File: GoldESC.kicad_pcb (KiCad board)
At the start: 2 copper layers, 2 parts, among them U10 LM5111-1M/NOPB, U20 PSMN1R0-30YLDX

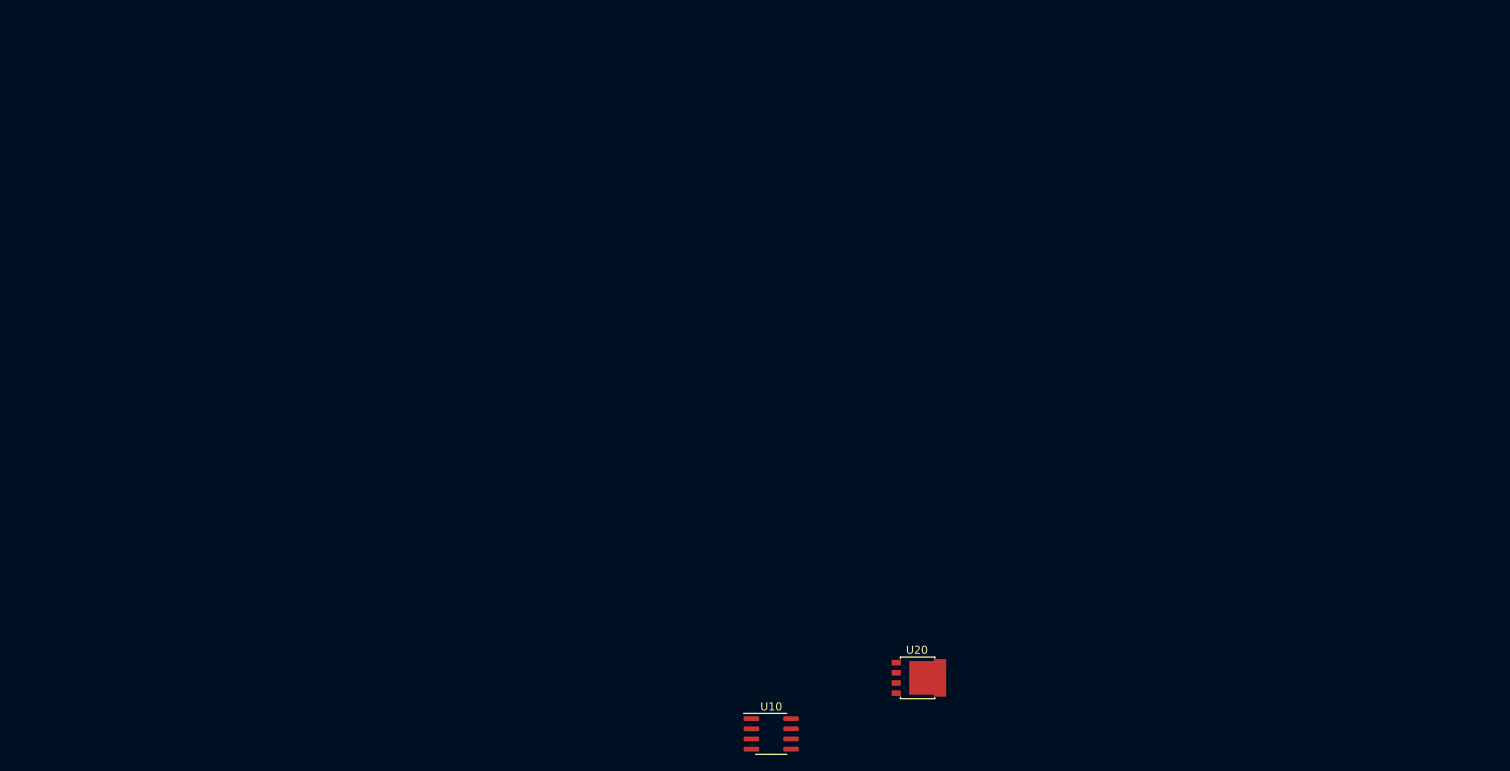
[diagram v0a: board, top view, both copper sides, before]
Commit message: Added fets and drivers, initial critical components selected
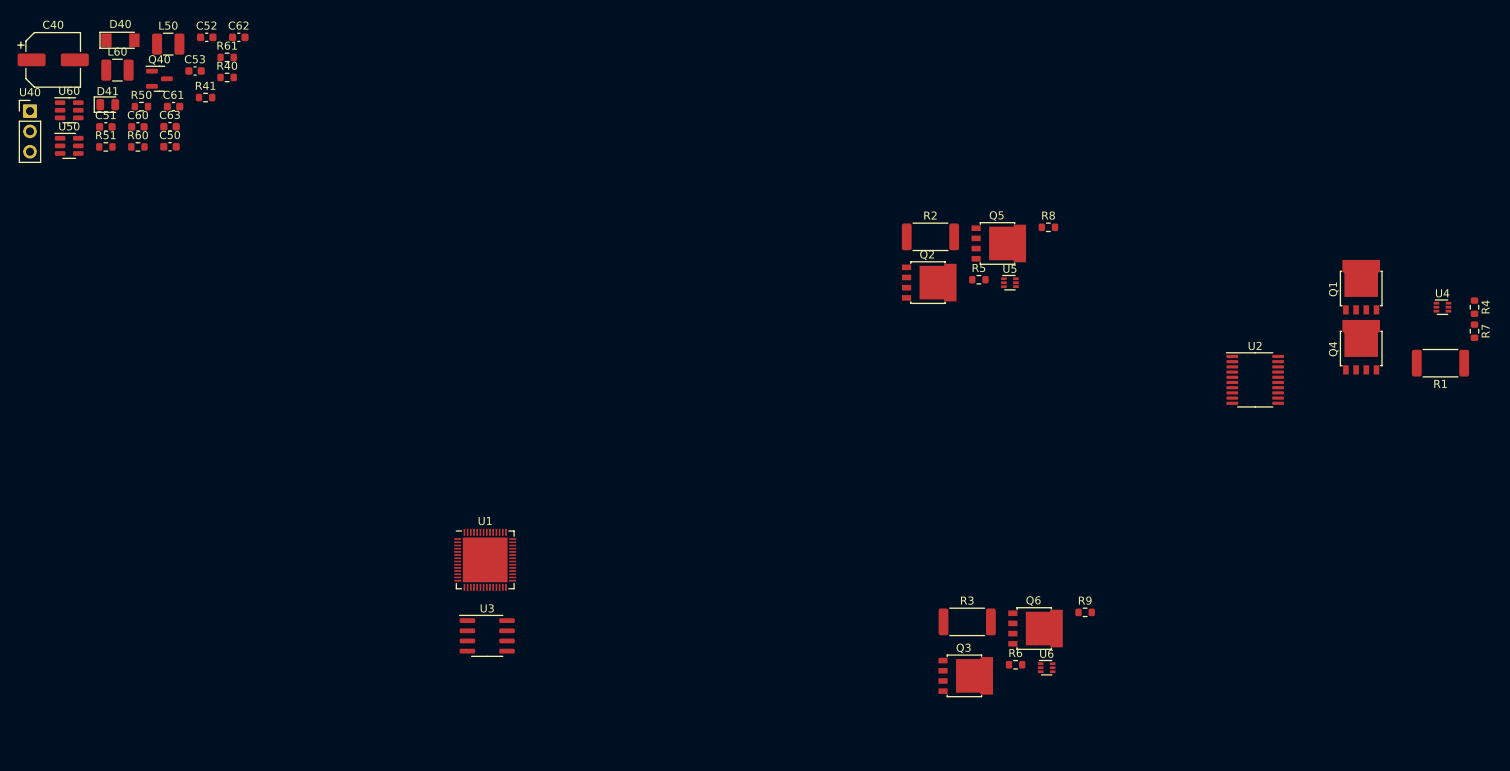
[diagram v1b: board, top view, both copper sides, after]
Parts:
- removed U10: LM5111-1M/NOPB, Package_SO:SOIC-8_3.9x4.9mm_P1.27mm
- removed U20: PSMN1R0-30YLDX, Package_TO_SOT_SMD:LFPAK56
- added C40: 100uF, Capacitor_SMD:CP_Elec_6.3x7.7, F.Cu at (55.2, 11.2)
- added C50: 10uF, Capacitor_SMD:C_0603_1608Metric, F.Cu at (69.8, 22.1)
- added C51: 100nF, Capacitor_SMD:C_0603_1608Metric, F.Cu at (61.8, 19.6)
- added C52: 22pF, Capacitor_SMD:C_0603_1608Metric, F.Cu at (74.4, 8.43)
- added C53: 22uF, Capacitor_SMD:C_0603_1608Metric, F.Cu at (73.0, 12.6)
- added C60: 10uF, Capacitor_SMD:C_0603_1608Metric, F.Cu at (65.8, 19.6)
- added C61: 100nF, Capacitor_SMD:C_0603_1608Metric, F.Cu at (70.3, 17.1)
- added C62: 22pF, Capacitor_SMD:C_0603_1608Metric, F.Cu at (78.5, 8.43)
- added C63: 22uF, Capacitor_SMD:C_0603_1608Metric, F.Cu at (69.8, 19.6)
- added D40: ZMM5V6, Diode_SMD:D_MiniMELF, F.Cu at (63.6, 8.80)
- added D41: POWER_LED, LED_SMD:LED_0805_2012Metric, F.Cu at (62.1, 16.8)
- added L50: 4.7uH, Inductor_SMD:L_1210_3225Metric, F.Cu at (69.6, 9.28)
- added L60: 4.7uH, Inductor_SMD:L_1210_3225Metric, F.Cu at (63.3, 12.5)
- added Q1: YJG150N03A, Package_TO_SOT_SMD:LFPAK56, F.Cu at (218.8, 39.7)
- added Q2: YJG150N03A, Package_TO_SOT_SMD:LFPAK56, F.Cu at (164.8, 39.1)
- added Q3: YJG150N03A, Package_TO_SOT_SMD:LFPAK56, F.Cu at (169.3, 88.2)
- added Q4: YJG150N03A, Package_TO_SOT_SMD:LFPAK56, F.Cu at (218.8, 47.2)
- added Q40: AO3401A, Package_TO_SOT_SMD:SOT-23, F.Cu at (68.5, 13.6)
- added Q5: YJG150N03A, Package_TO_SOT_SMD:LFPAK56, F.Cu at (173.4, 34.2)
- added Q6: YJG150N03A, Package_TO_SOT_SMD:LFPAK56, F.Cu at (178.0, 82.3)
- added R1: 0.5mR, Resistor_SMD:R_2512_6332Metric, F.Cu at (228.7, 49.2)
- added R2: 0.5mR, Resistor_SMD:R_2512_6332Metric, F.Cu at (164.9, 33.4)
- added R3: 0.5mR, Resistor_SMD:R_2512_6332Metric, F.Cu at (169.5, 81.5)
- added R4: R?, Resistor_SMD:R_0603_1608Metric, F.Cu at (232.9, 42.2)
- added R40: 10K, Resistor_SMD:R_0603_1608Metric, F.Cu at (77.0, 13.4)
- added R41: 1K, Resistor_SMD:R_0603_1608Metric, F.Cu at (74.3, 16.0)
- added R5: R?, Resistor_SMD:R_0603_1608Metric, F.Cu at (171.0, 38.7)
- added R50: 100K, Resistor_SMD:R_0603_1608Metric, F.Cu at (66.3, 17.1)
- added R51: 22K, Resistor_SMD:R_0603_1608Metric, F.Cu at (61.8, 22.1)
- added R6: R?, Resistor_SMD:R_0603_1608Metric, F.Cu at (175.6, 86.9)
- added R60: 100K, Resistor_SMD:R_0603_1608Metric, F.Cu at (65.8, 22.1)
- added R61: 13K, Resistor_SMD:R_0603_1608Metric, F.Cu at (77.0, 10.9)
- added R7: R?, Resistor_SMD:R_0603_1608Metric, F.Cu at (232.9, 45.2)
- added R8: R?, Resistor_SMD:R_0603_1608Metric, F.Cu at (179.7, 32.2)
- added R9: R?, Resistor_SMD:R_0603_1608Metric, F.Cu at (184.2, 80.3)
- added U1: ESP32-S2, Package_DFN_QFN:QFN-56-1EP_7x7mm_P0.4mm_EP5.6x5.6mm, F.Cu at (109.2, 73.8)
- added U2: DRV8300NIPWR, Package_SO:TSSOP-20_4.4x6.5mm_P0.65mm, F.Cu at (205.5, 51.2)
- added U3: MCP2551-I-SN, Package_SO:SOIC-8_3.9x4.9mm_P1.27mm, F.Cu at (109.5, 83.2)
- added U4: INA185A, Package_TO_SOT_SMD:SOT-563, F.Cu at (228.9, 42.2)
- added U40: Switch1SPDT, Connector_PinHeader_2.54mm:PinHeader_1x03_P2.54mm_Vertical, F.Cu at (52.4, 17.6)
- added U5: INA185A, Package_TO_SOT_SMD:SOT-563, F.Cu at (174.8, 39.1)
- added U50: SY8113BADC, Package_TO_SOT_SMD:TSOT-23-6, F.Cu at (57.2, 22.0)
- added U6: INA185A, Package_TO_SOT_SMD:SOT-563, F.Cu at (179.4, 87.2)
- added U60: SY8113BADC, Package_TO_SOT_SMD:TSOT-23-6, F.Cu at (57.2, 17.6)

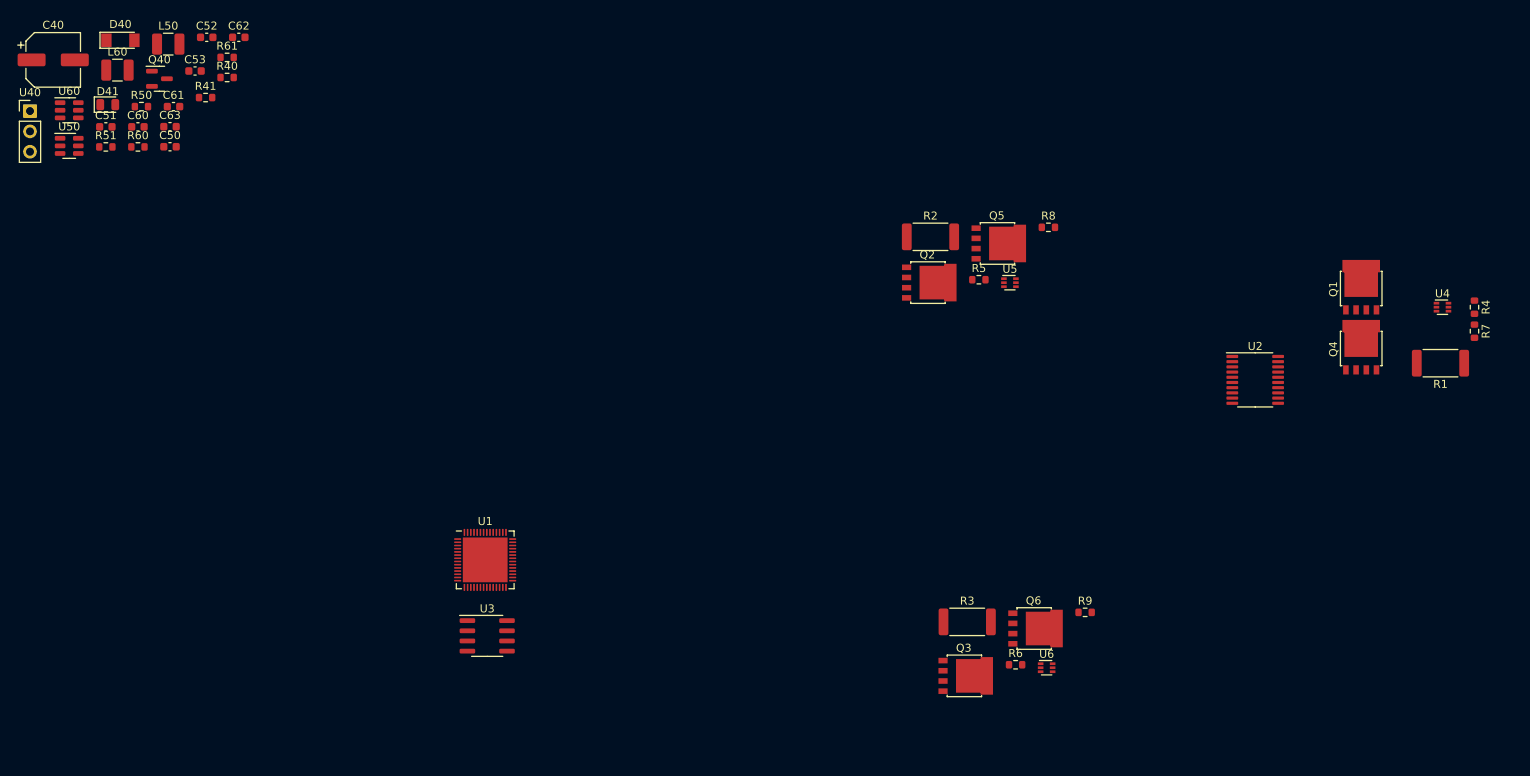
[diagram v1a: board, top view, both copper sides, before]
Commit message: moved the Dsub off-board, most of initial layout routed
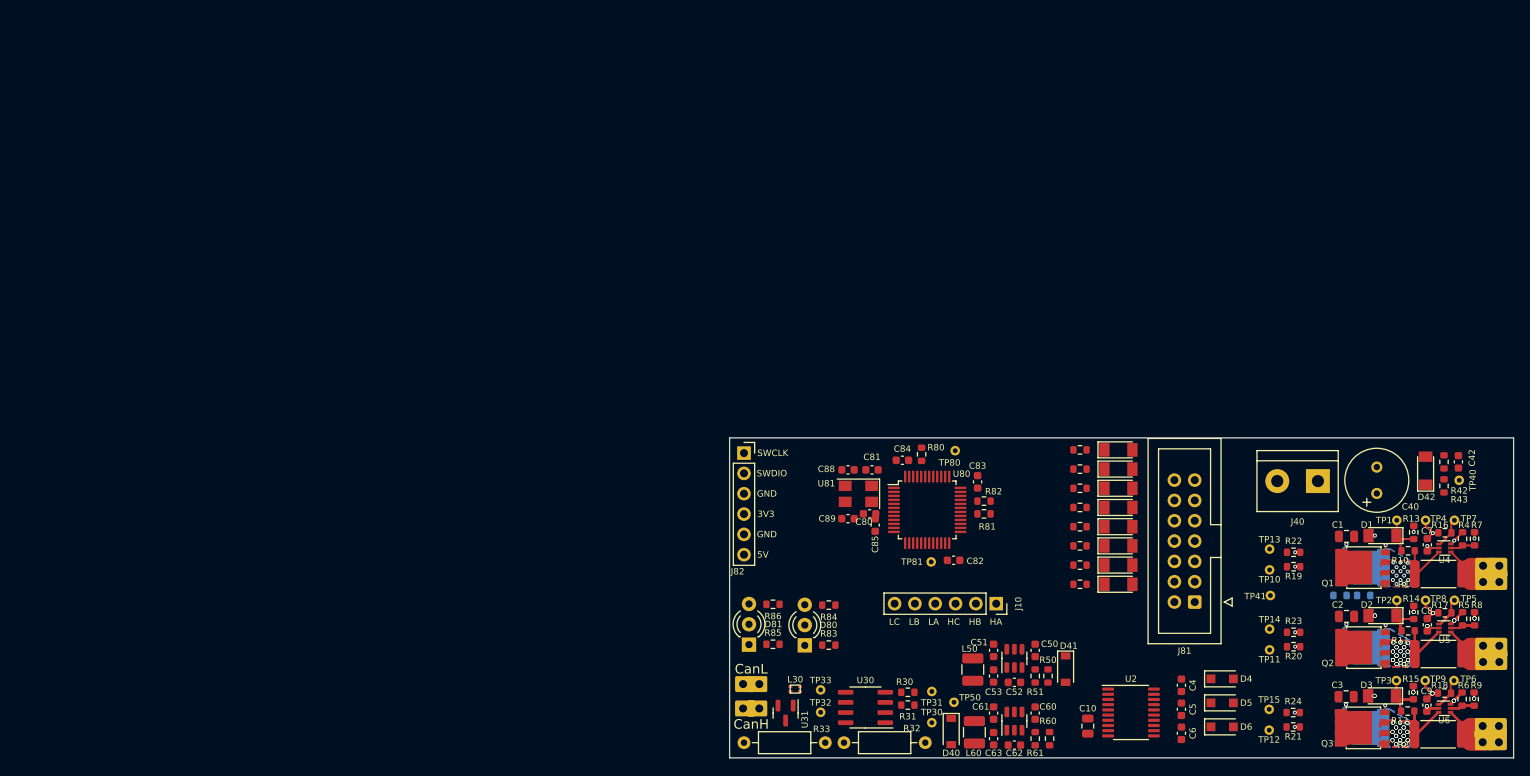
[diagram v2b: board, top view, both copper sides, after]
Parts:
- removed Q40: AO3401A, Package_TO_SOT_SMD:SOT-23
- removed U1: ESP32-S2, Package_DFN_QFN:QFN-56-1EP_7x7mm_P0.4mm_EP5.6x5.6mm
- removed U3: MCP2551-I-SN, Package_SO:SOIC-8_3.9x4.9mm_P1.27mm
- removed U40: Switch1SPDT, Connector_PinHeader_2.54mm:PinHeader_1x03_P2.54mm_Vertical
- added C1: 10uF,25V, Capacitor_SMD:C_0805_2012Metric, F.Cu at (216.9, 70.8)
- added C10: 1uF?/24V?, Capacitor_SMD:C_0805_2012Metric, F.Cu at (184.6, 94.5)
- added C2: 10uF,25V, Capacitor_SMD:C_0805_2012Metric, F.Cu at (216.9, 80.8)
- added C3: 10uF,25V, Capacitor_SMD:C_0805_2012Metric, F.Cu at (216.9, 90.8)
- added C4: 470nF?/16V?, Capacitor_SMD:C_0603_1608Metric, F.Cu at (196.3, 89.4)
- added C42: 100nF, Capacitor_SMD:C_0603_1608Metric, F.Cu at (230.9, 61.5)
- added C5: 470nF?/16V?, Capacitor_SMD:C_0603_1608Metric, F.Cu at (196.3, 92.4)
- added C6: 470nF?/16V?, Capacitor_SMD:C_0603_1608Metric, F.Cu at (196.3, 95.4)
- added C7: 4.7nF, Capacitor_SMD:C_0603_1608Metric, F.Cu at (227.0, 71.9)
- added C8: 4.7nF, Capacitor_SMD:C_0603_1608Metric, F.Cu at (227.0, 81.9)
- added C80: 100nF, Capacitor_SMD:C_0603_1608Metric, F.Cu at (157.3, 68.0)
- added C81: 2.2uF, Capacitor_SMD:C_0603_1608Metric, F.Cu at (157.6, 62.5)
- added C82: 2.2uF, Capacitor_SMD:C_0603_1608Metric, F.Cu at (167.8, 73.8)
- added C83: 2.2uF, Capacitor_SMD:C_0603_1608Metric, F.Cu at (170.8, 64.0)
- added C84: 2.2uF, Capacitor_SMD:C_0603_1608Metric, F.Cu at (161.4, 61.3)
- added C85: 2.2uF, Capacitor_SMD:C_0603_1608Metric, F.Cu at (158.0, 69.4)
- added C88: 15pF, Capacitor_SMD:C_0603_1608Metric, F.Cu at (154.6, 62.5)
- added C89: 15pF, Capacitor_SMD:C_0603_1608Metric, F.Cu at (154.6, 68.6)
- added C9: 4.7nF, Capacitor_SMD:C_0603_1608Metric, F.Cu at (227.0, 91.9)
- added D1: ZMM3V3, Diode_SMD:D_MiniMELF, F.Cu at (221.4, 70.7)
- added D2: ZMM3V3, Diode_SMD:D_MiniMELF, F.Cu at (221.4, 80.7)
- added D3: ZMM3V3, Diode_SMD:D_MiniMELF, F.Cu at (221.4, 90.8)
- added D4: CRH01, Diode_SMD:D_SOD-123F, F.Cu at (201.4, 88.6)
- added D42: ZMM3V3, Diode_SMD:D_MiniMELF, F.Cu at (226.8, 62.6)
- added D5: CRH01, Diode_SMD:D_SOD-123F, F.Cu at (201.4, 91.6)
- added D6: CRH01, Diode_SMD:D_SOD-123F, F.Cu at (201.4, 94.6)
- added D70: Z3V3, Diode_SMD:D_MiniMELF, F.Cu at (188.4, 74.4)
- added D71: Z3V3, Diode_SMD:D_MiniMELF, F.Cu at (188.4, 76.8)
- added D72: Z3V3, Diode_SMD:D_MiniMELF, F.Cu at (188.4, 64.8)
- added D73: Z3V3, Diode_SMD:D_MiniMELF, F.Cu at (188.4, 62.4)
- added D74: Z3V3, Diode_SMD:D_MiniMELF, F.Cu at (188.4, 72.0)
- added D75: Z3V3, Diode_SMD:D_MiniMELF, F.Cu at (188.4, 67.2)
- added D76: Z3V3, Diode_SMD:D_MiniMELF, F.Cu at (188.4, 69.6)
- added D77: Z3V3, Diode_SMD:D_MiniMELF, F.Cu at (188.4, 60.0)
- added D80: LED_Dual_AKA, LED_THT:LED_D3.0mm-3, F.Cu at (149.2, 84.4)
- added D81: LED_Dual_AKA, LED_THT:LED_D3.0mm-3, F.Cu at (142.2, 84.3)
- added J1: PhaseOut, AlfredoFootprints:TGD_ESC_PwrPad, F.Cu at (235.0, 75.5)
- added J10: Conn_01x06, Connector_PinSocket_2.54mm:PinSocket_1x06_P2.54mm_Vertical, F.Cu at (173.1, 79.2)
- added J2: PhaseOut, AlfredoFootprints:TGD_ESC_PwrPad, F.Cu at (235.0, 85.5)
- added J3: PhaseOut, AlfredoFootprints:TGD_ESC_PwrPad, F.Cu at (234.9, 95.5)
- added J30: CanOut, AlfredoFootprints:TGD_ESC_SigPads, F.Cu at (143.5, 89.3)
- added J40: Supply, TerminalBlock:TerminalBlock_bornier-2_P5.08mm, F.Cu at (213.3, 63.9)
- added J81: Conn_02x07_Counter_Clockwise, Connector_IDC:IDC-Header_2x07_P2.54mm_Vertical, F.Cu at (197.9, 79.0)
- added J82: Conn_01x06, Connector_PinSocket_2.54mm:PinSocket_1x06_P2.54mm_Vertical, F.Cu at (141.6, 60.4)
- added L30: KCZ1210, AlfredoFootprints:KCZ1210, F.Cu at (148.0, 89.9)
- added R10: 15K, Resistor_SMD:R_0603_1608Metric, F.Cu at (224.6, 72.6)
- added R11: 15K, Resistor_SMD:R_0603_1608Metric, F.Cu at (224.6, 82.6)
- added R12: 15K, Resistor_SMD:R_0603_1608Metric, F.Cu at (224.6, 92.7)
- added R13: 2K2, Resistor_SMD:R_0603_1608Metric, F.Cu at (225.3, 70.3)
- added R14: 2K2, Resistor_SMD:R_0603_1608Metric, F.Cu at (225.3, 80.3)
- added R15: 2K2, Resistor_SMD:R_0603_1608Metric, F.Cu at (225.3, 90.3)
- added R16: 100R, Resistor_SMD:R_0603_1608Metric, F.Cu at (229.2, 70.4)
- added R17: 100R, Resistor_SMD:R_0603_1608Metric, F.Cu at (229.2, 80.4)
- added R18: 100R, Resistor_SMD:R_0603_1608Metric, F.Cu at (229.2, 90.4)
- added R19: 2R2?, Resistor_SMD:R_0603_1608Metric, F.Cu at (210.3, 74.6)
- added R20: 2R2?, Resistor_SMD:R_0603_1608Metric, F.Cu at (210.3, 84.6)
- added R21: 2R2?, Resistor_SMD:R_0603_1608Metric, F.Cu at (210.2, 94.6)
- added R22: 2R2?, Resistor_SMD:R_0603_1608Metric, F.Cu at (210.3, 72.8)
- added R23: 2R2?, Resistor_SMD:R_0603_1608Metric, F.Cu at (210.3, 82.8)
- added R24: 2R2?, Resistor_SMD:R_0603_1608Metric, F.Cu at (210.2, 92.8)
- added R30: 6K, Resistor_SMD:R_0603_1608Metric, F.Cu at (162.1, 90.3)
- added R31: 10K, Resistor_SMD:R_0603_1608Metric, F.Cu at (162.1, 91.9)
- added R32: 50K?, Resistor_THT:R_Axial_DIN0207_L6.3mm_D2.5mm_P10.16mm_Horizontal, F.Cu at (154.1, 96.6)
- added R33: 120R?, Resistor_THT:R_Axial_DIN0207_L6.3mm_D2.5mm_P10.16mm_Horizontal, F.Cu at (141.6, 96.6)
- added R42: 2K2, Resistor_SMD:R_0603_1608Metric, F.Cu at (229.1, 61.5)
- added R43: 15K, Resistor_SMD:R_0603_1608Metric, F.Cu at (229.1, 64.5)
- added R70: 2K2, Resistor_SMD:R_0603_1608Metric, F.Cu at (183.6, 74.4)
- added R71: 2K2, Resistor_SMD:R_0603_1608Metric, F.Cu at (183.6, 76.8)
- added R72: 2K2, Resistor_SMD:R_0603_1608Metric, F.Cu at (183.6, 64.8)
- added R73: 2K2, Resistor_SMD:R_0603_1608Metric, F.Cu at (183.6, 62.4)
- added R74: 2K2, Resistor_SMD:R_0603_1608Metric, F.Cu at (183.6, 72.0)
- added R75: 2K2, Resistor_SMD:R_0603_1608Metric, F.Cu at (183.6, 67.2)
- added R76: 2K2, Resistor_SMD:R_0603_1608Metric, F.Cu at (183.6, 69.6)
- added R77: 2K2, Resistor_SMD:R_0603_1608Metric, F.Cu at (183.6, 60.0)
- added R80: 10K, Resistor_SMD:R_0603_1608Metric, F.Cu at (163.8, 60.5)
- added R81: 22R, Resistor_SMD:R_0603_1608Metric, F.Cu at (171.6, 68.0)
- added R82: 22R, Resistor_SMD:R_0603_1608Metric, F.Cu at (171.6, 66.4)
- added R83: 200R, Resistor_SMD:R_0603_1608Metric, F.Cu at (152.2, 84.4)
- added R84: 200R, Resistor_SMD:R_0603_1608Metric, F.Cu at (152.2, 79.4)
- added R85: 200R, Resistor_SMD:R_0603_1608Metric, F.Cu at (145.2, 84.3)
- added R86: 200R, Resistor_SMD:R_0603_1608Metric, F.Cu at (145.2, 79.3)
- added TP1: TestPoint, AlfredoFootprints:GE_TestPoint_Loop, F.Cu at (223.2, 68.8)
- added TP10: TestPoint, AlfredoFootprints:GE_TestPoint_Loop, F.Cu at (207.3, 75.0)
- added TP11: TestPoint, AlfredoFootprints:GE_TestPoint_Loop, F.Cu at (207.3, 85.0)
- added TP12: TestPoint, AlfredoFootprints:GE_TestPoint_Loop, F.Cu at (207.2, 95.0)
- added TP13: TestPoint, AlfredoFootprints:GE_TestPoint_Loop, F.Cu at (207.3, 72.4)
- added TP14: TestPoint, AlfredoFootprints:GE_TestPoint_Loop, F.Cu at (207.3, 82.4)
- added TP15: TestPoint, AlfredoFootprints:GE_TestPoint_Loop, F.Cu at (207.2, 92.4)
- added TP2: TestPoint, AlfredoFootprints:GE_TestPoint_Loop, F.Cu at (223.2, 78.8)
- added TP3: TestPoint, AlfredoFootprints:GE_TestPoint_Loop, F.Cu at (223.1, 88.8)
- added TP30: TestPoint, AlfredoFootprints:GE_TestPoint_Loop, F.Cu at (165.1, 94.1)
- added TP31: TestPoint, AlfredoFootprints:GE_TestPoint_Loop, F.Cu at (165.1, 90.2)
- added TP32: TestPoint, AlfredoFootprints:GE_TestPoint_Loop, F.Cu at (151.2, 92.8)
- added TP33: TestPoint, AlfredoFootprints:GE_TestPoint_Loop, F.Cu at (151.2, 90.0)
- added TP4: TestPoint, AlfredoFootprints:GE_TestPoint_Loop, F.Cu at (226.8, 68.8)
- added TP40: TestPoint, AlfredoFootprints:GE_TestPoint_Loop, F.Cu at (231.0, 63.8)
- added TP41: TestPoint, AlfredoFootprints:GE_TestPoint_Loop, F.Cu at (207.4, 78.2)
- added TP5: TestPoint, AlfredoFootprints:GE_TestPoint_Loop, F.Cu at (230.4, 78.8)
- added TP50: TestPoint, AlfredoFootprints:GE_TestPoint_Loop, F.Cu at (167.8, 91.5)
- added TP6: TestPoint, AlfredoFootprints:GE_TestPoint_Loop, F.Cu at (230.3, 88.8)
- added TP7: TestPoint, AlfredoFootprints:GE_TestPoint_Loop, F.Cu at (230.4, 68.8)
- added TP8: TestPoint, AlfredoFootprints:GE_TestPoint_Loop, F.Cu at (226.8, 78.8)
- added TP80: TestPoint, AlfredoFootprints:GE_TestPoint_Loop, F.Cu at (168.0, 60.1)
- added TP81: TestPoint, AlfredoFootprints:GE_TestPoint_Loop, F.Cu at (165.0, 74.0)
- added TP9: TestPoint, AlfredoFootprints:GE_TestPoint_Loop, F.Cu at (226.7, 88.8)
- added U30: MCP2551-I-SN, Package_SO:SOIC-8_3.9x4.9mm_P1.27mm, F.Cu at (156.8, 92.2)
- added U31: CPDT-12V, Package_TO_SOT_SMD:SOT-23, F.Cu at (146.8, 92.9)
- added U80: STM32F103C8Tx, Package_QFP:LQFP-48_7x7mm_P0.5mm, F.Cu at (164.5, 67.5)
- added U81: Crystal_GND3, Crystal:Crystal_SMD_5032-4Pin_5.0x3.2mm, F.Cu at (155.9, 65.5)
- C40: value 100uF -> 330uF; footprint Capacitor_SMD:CP_Elec_6.3x7.7 -> AlfredoFootprints:TGD_lowESR_cap
- D40: value ZMM5V6 -> B5819W; footprint Diode_SMD:D_MiniMELF -> Diode_SMD:D_SOD-123
- D41: value POWER_LED -> B5819W; footprint LED_SMD:LED_0805_2012Metric -> Diode_SMD:D_SOD-123
- Q4, Q5, Q6, R40: moved to B.Cu
- R4, R5, R6, R7, R8, R9: value R? -> 1K
- R41: value 1K -> 10K RTC; moved to B.Cu
- U4, U5, U6: value INA185A -> INA185A1
- moved C40 173.6 mm to (220.7, 63.8), turned to 90 degrees
- moved R41 157.6 mm to (219.1, 78.2), turned to 180 degrees
- moved R40 153.4 mm to (216.1, 78.2), turned to 180 degrees
- moved U60 140.7 mm to (175.4, 93.9), turned to 90 degrees
- moved D41 139.0 mm to (181.8, 87.4), turned to -90 degrees
- moved R60 135.9 mm to (179.8, 96.1), turned to 90 degrees
- moved L60 135.4 mm to (170.4, 95.3), turned to -90 degrees
- moved D40 135.1 mm to (167.5, 95.2), turned to -90 degrees
- moved U50 134.4 mm to (175.4, 86.1), turned to 90 degrees
- moved C60 134.0 mm to (178.0, 92.9), turned to 90 degrees
- moved R50 133.8 mm to (179.6, 88.3), turned to -90 degrees
- moved R51 133.7 mm to (178.0, 88.3), turned to 90 degrees
- moved R61 132.1 mm to (178.0, 96.1), turned to 90 degrees
- moved C62 131.2 mm to (175.4, 96.9), turned to 180 degrees
- moved C52 129.2 mm to (175.4, 89.1), turned to 180 degrees
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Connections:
- net /GE-Fets-A/PHx renamed Net-(J1-Pad1)
- net /GE-Fets-B/PHx renamed Net-(J2-Pad1)
- net /GE-Fets-C/PHx renamed Net-(J3-Pad1)
- C50 pad 2: VDD -> Net-(C50-Pad2)
- D40 pad 1: VDD -> Net-(C50-Pad2)
- D40 pad 2: Net-(D40-Pad2) -> +5V
- D41 pad 1: Net-(D41-Pad1) -> Net-(C50-Pad2)
- D41 pad 2: +3V3 -> VDD
- Q1 pad 4: /GE-Fets-A/GHx -> Net-(Q1-Pad4)
- Q2 pad 4: /GE-Fets-B/GHx -> Net-(Q2-Pad4)
- Q3 pad 4: /GE-Fets-C/GHx -> Net-(Q3-Pad4)
- Q4 pad 4: /GE-Fets-A/GLx -> Net-(Q4-Pad4)
- Q5 pad 4: /GE-Fets-B/GLx -> Net-(Q5-Pad4)
- Q6 pad 4: /GE-Fets-C/GLx -> Net-(Q6-Pad4)
- R40 pad 1: Net-(D40-Pad2) -> TEMP_FETS
- R41 pad 1: GND -> +3V3
- R41 pad 2: Net-(D41-Pad1) -> TEMP_FETS
- U2 pad 1: unconnected-(U2-Pad1) -> INHA
- U2 pad 14: unconnected-(U2-Pad14) -> Net-(C6-Pad1)
- U2 pad 17: unconnected-(U2-Pad17) -> Net-(C5-Pad1)
- U2 pad 2: unconnected-(U2-Pad2) -> INHB
- U2 pad 20: unconnected-(U2-Pad20) -> Net-(C4-Pad1)
- U2 pad 3: unconnected-(U2-Pad3) -> INHC
- U2 pad 4: unconnected-(U2-Pad4) -> INLA
- U2 pad 5: unconnected-(U2-Pad5) -> INLB
- U2 pad 6: unconnected-(U2-Pad6) -> INLC
- U2 pad 7: unconnected-(U2-Pad7) -> VDD
- U2 pad 8: unconnected-(U2-Pad8) -> GND
- U4 pad 1: /GE-Fets-A/CURx -> Net-(R16-Pad2)
- U5 pad 1: /GE-Fets-B/CURx -> Net-(R17-Pad2)
- U50 pad 4: VDD -> Net-(C50-Pad2)
- U50 pad 5: VDD -> Net-(C50-Pad2)
- U6 pad 1: /GE-Fets-C/CURx -> Net-(R18-Pad2)
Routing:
- net GND: track 0.00 -> 31.7 mm, vias 0 -> 28
- net Net-(J2-Pad1): track 0.00 -> 22.8 mm
- net Net-(J3-Pad1): track 0.00 -> 22.8 mm
- net /GE-Fets-B/SHx: track 0.00 -> 21.2 mm, vias 0 -> 45
- net /GE-Fets-C/SHx: track 0.00 -> 21.2 mm, vias 0 -> 45
- net sVLT_B: track 0.00 -> 15.4 mm
- net sVLT_C: track 0.00 -> 15.4 mm
- net +3V3: track 0.00 -> 14.5 mm, vias 0 -> 7
- net Net-(J1-Pad1): track 0.00 -> 9.72 mm
- net Net-(R6-Pad2): track 0.00 -> 9.25 mm
- net Net-(R5-Pad2): track 0.00 -> 9.25 mm
- net Net-(R18-Pad2): track 0.00 -> 8.21 mm
- net Net-(R17-Pad2): track 0.00 -> 8.21 mm
- net /GE-Fets-A/SHx: track 0.00 -> 7.06 mm, vias 0 -> 15
- net sCUR_C: track 0.00 -> 7.00 mm, vias 0 -> 3
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- added copper zone on B.Cu, net /GE-Fets-A/SHx
- added copper zone on F.Cu, net /GE-Fets-A/SHx
- added copper zone on B.Cu, net /GE-Fets-B/SHx
- added copper zone on F.Cu, net /GE-Fets-B/SHx
- added copper zone on B.Cu, net /GE-Fets-C/SHx
- added copper zone on F.Cu, net /GE-Fets-C/SHx
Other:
- board outline added: 98 x 40 mm
- copper layers 2 -> 4
- board text added: "3V3"
- board text added: "5V"
- board text added: "CanH"
- board text added: "CanL"
- board text added: "GND"
- board text added: "HA"
- board text added: "HB"
- board text added: "HC"
- board text added: "LA"
- board text added: "LB"
- board text added: "LC"
- board text added: "SWCLK"
- board text added: "SWDIO"

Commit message: GoldESC V1 ordered gerbers
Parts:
- added ?: , , F.Cu at (163.0, 85.8)
- added ?: , , F.Cu at (236.1, 67.0)
- added ?: , , F.Cu at (203.2, 76.3)
- added G***: LOGO, AlfredoFootprints:Alfredo_logo_small, B.Cu at (232.8, 66.5)
- moved TP81 7.64 mm to (172.2, 71.5), turned to 180 degrees
- moved TP80 6.52 mm to (161.5, 59.6)
- moved J40 5.18 mm to (208.2, 63.7), turned to 0 degrees
- moved D71 2.20 mm to (188.3, 79.0)
- moved R71 2.20 mm to (183.5, 79.0)
- moved D70 2.20 mm to (188.3, 76.6)
- moved R70 2.20 mm to (183.5, 76.6)
- moved C85 1.30 mm to (157.9, 70.7)
- moved C89 0.67 mm to (154.0, 68.3)
- moved C80 0.32 mm to (157.2, 68.3), turned to 180 degrees
- moved R19 0.05 mm to (210.2, 74.6)
- moved R20 0.05 mm to (210.2, 84.6)
- moved R22 0.05 mm to (210.2, 72.8)
- moved R23 0.05 mm to (210.2, 82.8)
- turned R50 to 90 degrees
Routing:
- net VDD: track 0.00 -> 158.0 mm
- net GND: track 31.7 -> 156.2 mm, vias 28 -> 41
- net +5V: track 0.00 -> 103.0 mm, vias 0 -> 6
- net sCUR_A: track 3.65 -> 92.7 mm
- net sVLT_VDD: track 0.00 -> 87.4 mm, vias 0 -> 1
- net sCUR_B: track 7.00 -> 92.5 mm, vias 3 -> 1
- net sVLT_A: track 6.42 -> 88.8 mm, vias 0 -> 1
- net sVLT_B: track 15.4 -> 95.8 mm, vias 0 -> 1
- net sCUR_C: track 7.00 -> 87.3 mm, vias 3 -> 1
- net sVLT_C: track 15.4 -> 92.5 mm, vias 0 -> 1
- net INLC: track 0.00 -> 67.2 mm, vias 0 -> 2
- net TEMP_FETS: track 0.00 -> 61.9 mm, vias 0 -> 1
- net INLA: track 0.00 -> 54.4 mm, vias 0 -> 2
- net INLB: track 0.00 -> 45.9 mm, vias 0 -> 2
- net /GE-Fets-A/GLx: track 0.00 -> 43.5 mm, vias 0 -> 1
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- added copper zone on In2.Cu, net +3V3
- added copper zone on B.Cu, net GND
- added copper zone on In1.Cu, net GND
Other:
- board text added: "A"
- board text added: "B"
- board text added: "C"
- board text added: "GoldESC V1 © Alfredo Systems 2022"

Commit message: Updated BOM
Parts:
- C10: value 1uF?/24V? -> 1uF
- C4, C5, C6: value 470nF?/16V? -> 1uF
- R19, R20, R21, R22, R23, R24: value 2R2? -> 15R
- R30: value 6K -> 5.6K
